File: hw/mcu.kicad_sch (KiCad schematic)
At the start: 2 parts, among them U1 ISP2454-LP-JT

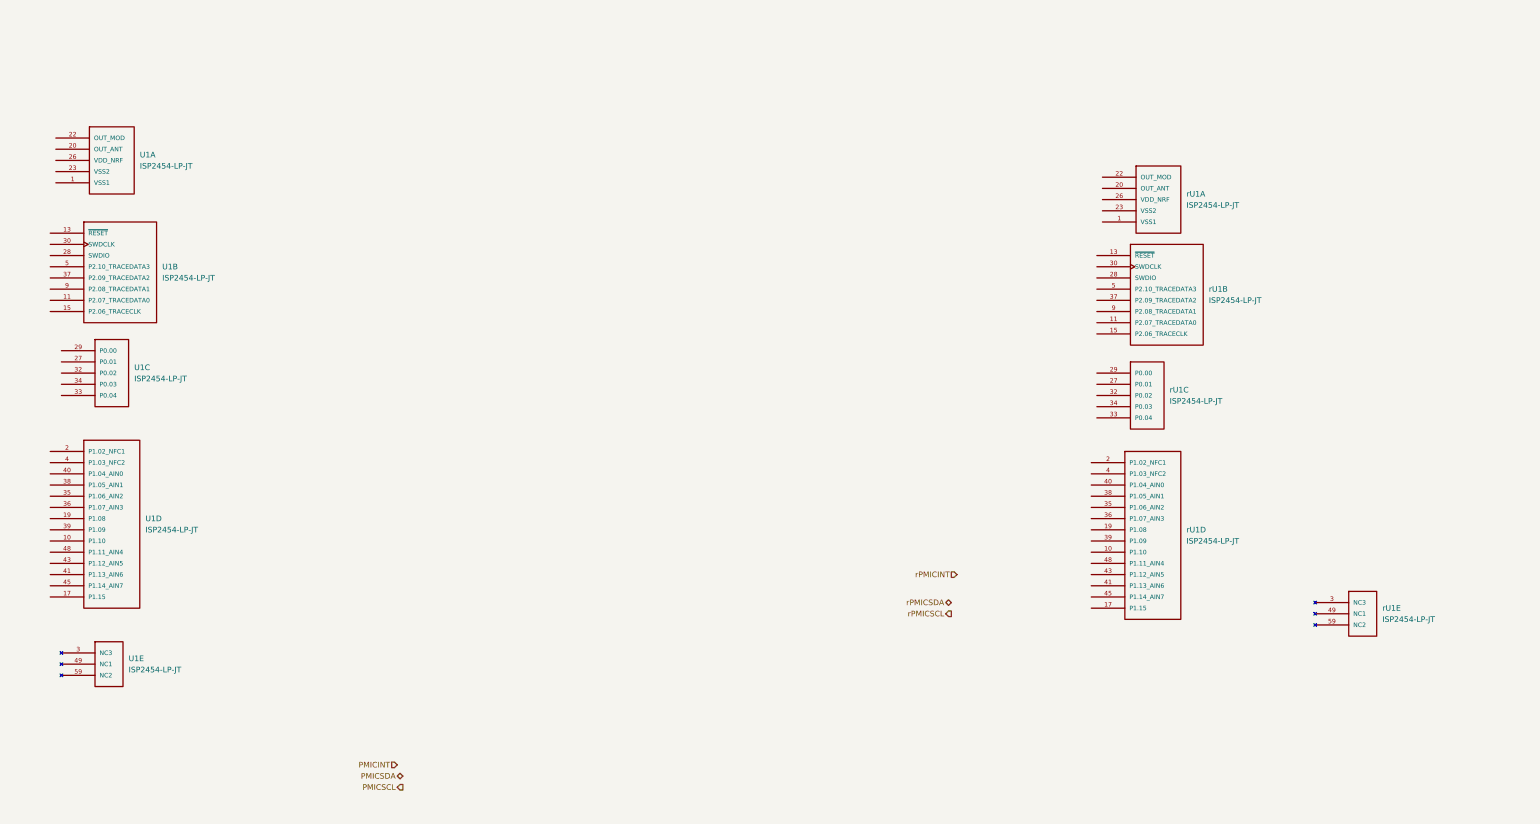
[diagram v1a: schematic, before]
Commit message: Hook up mcu
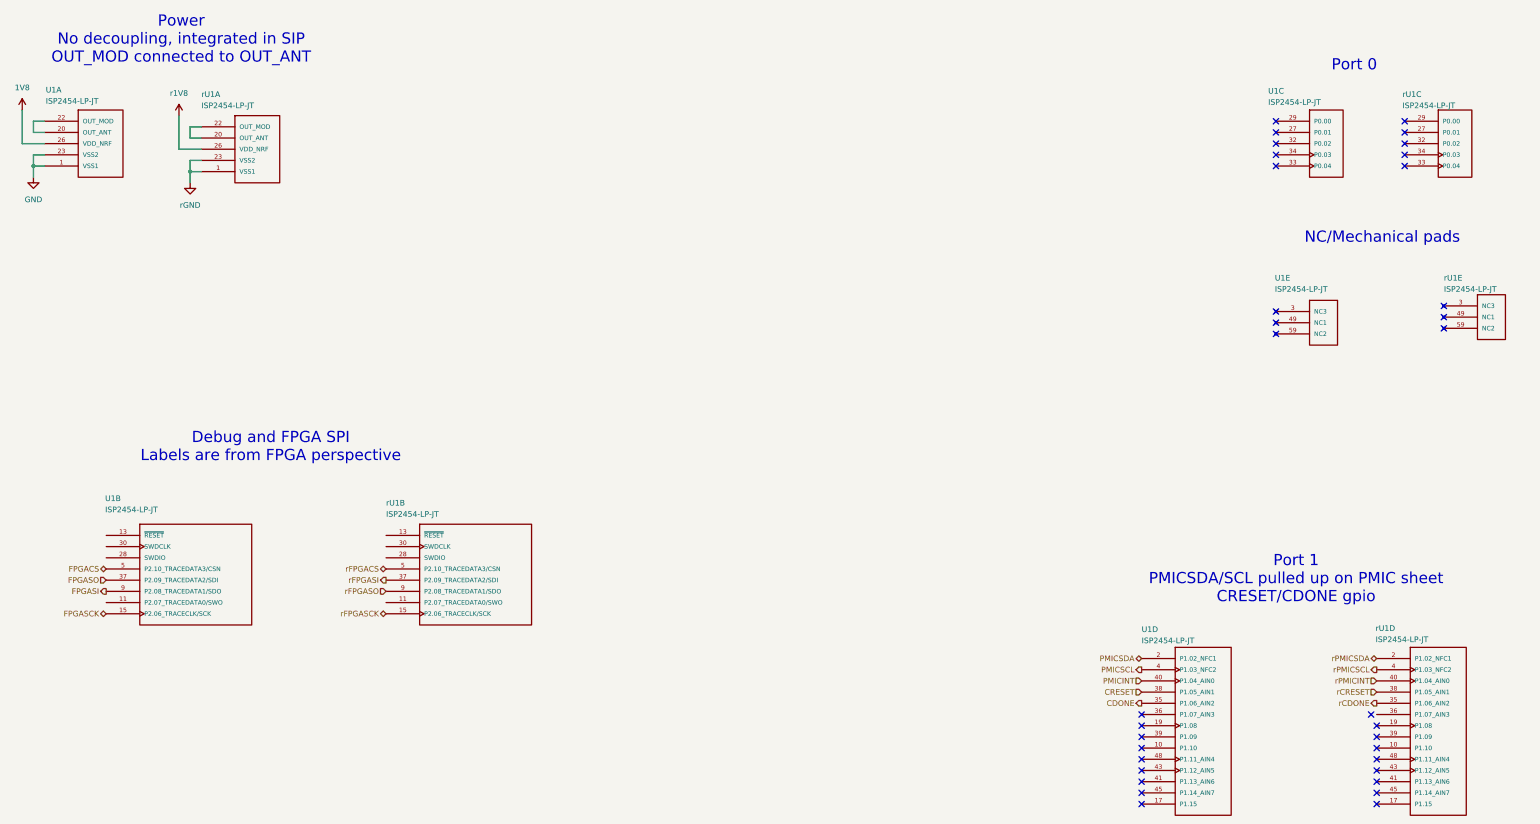
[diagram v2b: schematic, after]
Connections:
- net VSS2 is gone; now on net GND: U1.23 (VSS2), U1.24 (VSS2), U1.25 (VSS2), U1.31 (VSS2), rU1.23 (VSS2), rU1.24 (VSS2), rU1.25 (VSS2), rU1.31 (VSS2)
- net PMICINT: now also U1.40 (P1.04_AIN0)
- net PMICSCL: now also U1.4 (P1.03_NFC2)
- net PMICSDA: now also U1.2 (P1.02_NFC1)
- net rPMICINT: now also rU1.40 (P1.04_AIN0)
- net rPMICSCL: now also rU1.4 (P1.03_NFC2)
- net rPMICSDA: now also rU1.2 (P1.02_NFC1)
- net at rU1.20 (OUT_ANT): now also rU1.22 (OUT_MOD)
- net r1V8: now reaches rU1.26 (VDD_NRF)
- net CDONE: now reaches U1.35 (P1.06_AIN2)
- net CRESET: now reaches U1.38 (P1.05_AIN1)
- net rCDONE: now reaches rU1.35 (P1.06_AIN2)
- net rCRESET: now reaches rU1.38 (P1.05_AIN1)
- net FPGASCK: now reaches U1.15 (P2.06_TRACECLK/SCK)
- net FPGASO: now reaches U1.37 (P2.09_TRACEDATA2/SDI)
- net FPGACS: now reaches U1.5 (P2.10_TRACEDATA3/CSN)
- net FPGASI: now reaches U1.9 (P2.08_TRACEDATA1/SDO)
- net rFPGASCK: now reaches rU1.15 (P2.06_TRACECLK/SCK)
- net rFPGASI: now reaches rU1.37 (P2.09_TRACEDATA2/SDI)
- net rFPGACS: now reaches rU1.5 (P2.10_TRACEDATA3/CSN)
- net rFPGASO: now reaches rU1.9 (P2.08_TRACEDATA1/SDO)
- net at U1.20 (OUT_ANT): now also U1.22 (OUT_MOD)
- net 1V8: now reaches U1.26 (VDD_NRF)
- net VSS1 renamed GND
- no-connect marks 0 -> 34
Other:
- note added: "Debug and FPGA SPI Labels are from FPGA perspective"
- note added: "NC/Mechanical pads"
- note added: "Port 0"
- note added: "Port 1 PMICSDA/SCL pulled up on PMIC sheet CRESET/CDONE gpio"
- note added: "Power No decoupling, integrated in SIP OUT_MOD connected to OUT_ANT"
- moved on the sheet: U1A, U1E, rU1A, rU1E

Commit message: Sheet pins
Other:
- note added: "Port 1 PMICSDA/SCL pulled up on PMIC sheet CRESET/CDONE pulled up on FPGA sheet"
- note removed: "Port 1 PMICSDA/SCL pulled up on PMIC sheet CRESET/CDONE gpio"
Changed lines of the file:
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@@
 		)
 	)
-	(text "Port 1\nPMICSDA/SCL pulled up on PMIC sheet\nCRESET/CDONE gpio"
+	(text "Port 1\nPMICSDA/SCL pulled up on PMIC sheet\nCRESET/CDONE pulled up on FPGA sheet"
 		(exclude_from_sim no)
 		(at 333.502 149.606 0)
@@
 	)
 	(hierarchical_label "rCRESET"
+		(shape output)
+		(at 351.79 175.26 180)
+		(effects
+			(font
+				(size 1.27 1.27)
+			)
+			(justify right)
+		)
+	)
+	(hierarchical_label "CRESET"
+		(shape output)
+		(at 298.45 175.26 180)
+		(effects
+			(font
+				(size 1.27 1.27)
+			)
+			(justify right)
+		)
+	)
+	(hierarchical_label "PMICSCL"
+		(shape output)
+		(at 298.45 170.18 180)
+		(effects
+			(font
+				(size 1.27 1.27)
+			)
+			(justify right)
+		)
+	)
+	(hierarchical_label "rFPGASI"
+		(shape output)
+		(at 127 149.86 180)
+		(effects
+			(font
+				(size 1.27 1.27)
+			)
+			(justify right)
+		)
+	)
+	(hierarchical_label "CDONE"
 		(shape input)
-		(at 351.79 175.26 180)
-		(effects
-			(font
-				(size 1.27 1.27)
-			)
-			(justify right)
-		)
-	)
-	(hierarchical_label "CRESET"
-		(shape input)
-		(at 298.45 175.26 180)
-		(effects
-			(font
-				(size 1.27 1.27)
-			)
-			(justify right)
-		)
-	)
-	(hierarchical_label "PMICSCL"
-		(shape output)
-		(at 298.45 170.18 180)
-		(effects
-			(font
-				(size 1.27 1.27)
-			)
-			(justify right)
-		)
-	)
-	(hierarchical_label "rFPGASI"
-		(shape output)
-		(at 127 149.86 180)
-		(effects
-			(font
-				(size 1.27 1.27)
-			)
-			(justify right)
-		)
-	)
-	(hierarchical_label "CDONE"
-		(shape output)
 		(at 298.45 177.8 180)
 		(effects
@@
 	)
 	(hierarchical_label "rCDONE"
-		(shape output)
+		(shape input)
 		(at 351.79 177.8 180)
 		(effects

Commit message: Debug header
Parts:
- added J3, rJ3: TC2050-IDC, Alidade:TAG-CONNECT_TC2050-IDC, symbol Alidade:TC2050-IDC
- added R15, R16, R17, rR15, rR16, rR17: 10k, symbol Alidade:R
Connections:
- net 1V8: now also J3.1 (VREF), R15.1, R16.1
- net GND: now also J3.3 (GND), J3.5 (GND), J3.9 (GND), R17.2, rJ3.3 (GND), rJ3.5 (GND), rJ3.9 (GND), rR17.2
- net r1V8: now also rJ3.1 (VREF), rR15.1, rR16.1
- net SWO: now reaches U1.11 (P2.07_TRACEDATA0/SWO)
- net SWO: now also J3.6 (SWO)
- net NRST: now reaches U1.13 (~{RESET})
- net NRST: now also J3.10 (nRST), R16.2
- net SWDIO: now reaches U1.28 (SWDIO)
- net SWDIO: now also J3.2 (SWDIO), R15.2
- net SWCLK: now reaches U1.30 (SWDCLK)
- net SWCLK: now also J3.4 (SWDCLK), R17.1
- net rSWO: now reaches rU1.11 (P2.07_TRACEDATA0/SWO)
- net rSWO: now also rJ3.6 (SWO)
- net rNRST: now reaches rU1.13 (~{RESET})
- net rNRST: now also rJ3.10 (nRST), rR16.2
- net rSWDIO: now reaches rU1.28 (SWDIO)
- net rSWDIO: now also rJ3.2 (SWDIO), rR15.2
- net rSWCLK: now reaches rU1.30 (SWDCLK)
- net rSWCLK: now also rJ3.4 (SWDCLK), rR17.1
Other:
- note added: "Debug Header Pull up SWDIO, NRST Pull down SWCLK"
- title: (none) -> Alidade
- moved on the sheet: U1B, rU1B

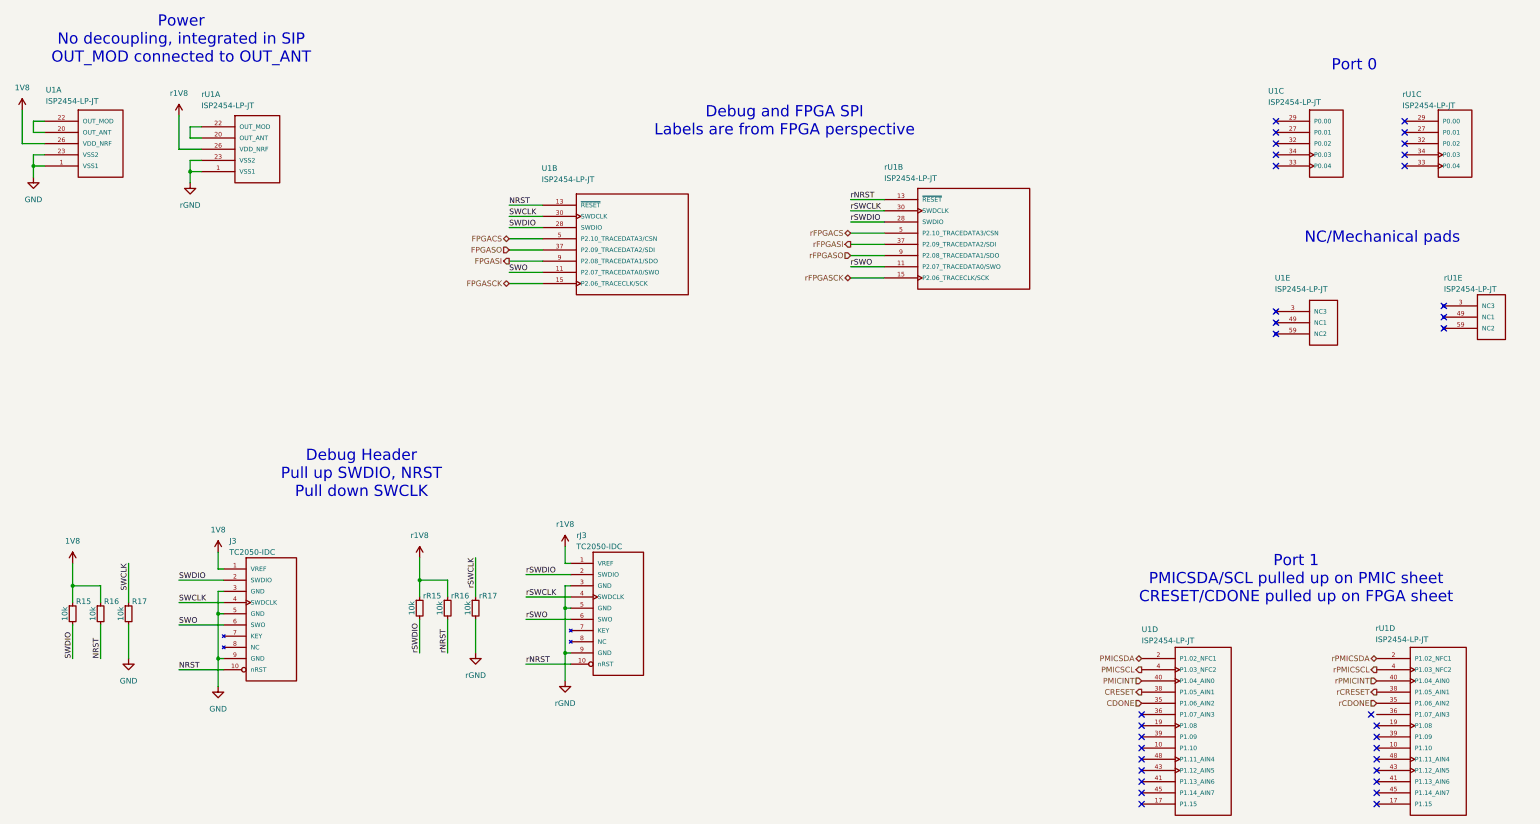
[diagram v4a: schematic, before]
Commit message: mcu page erc
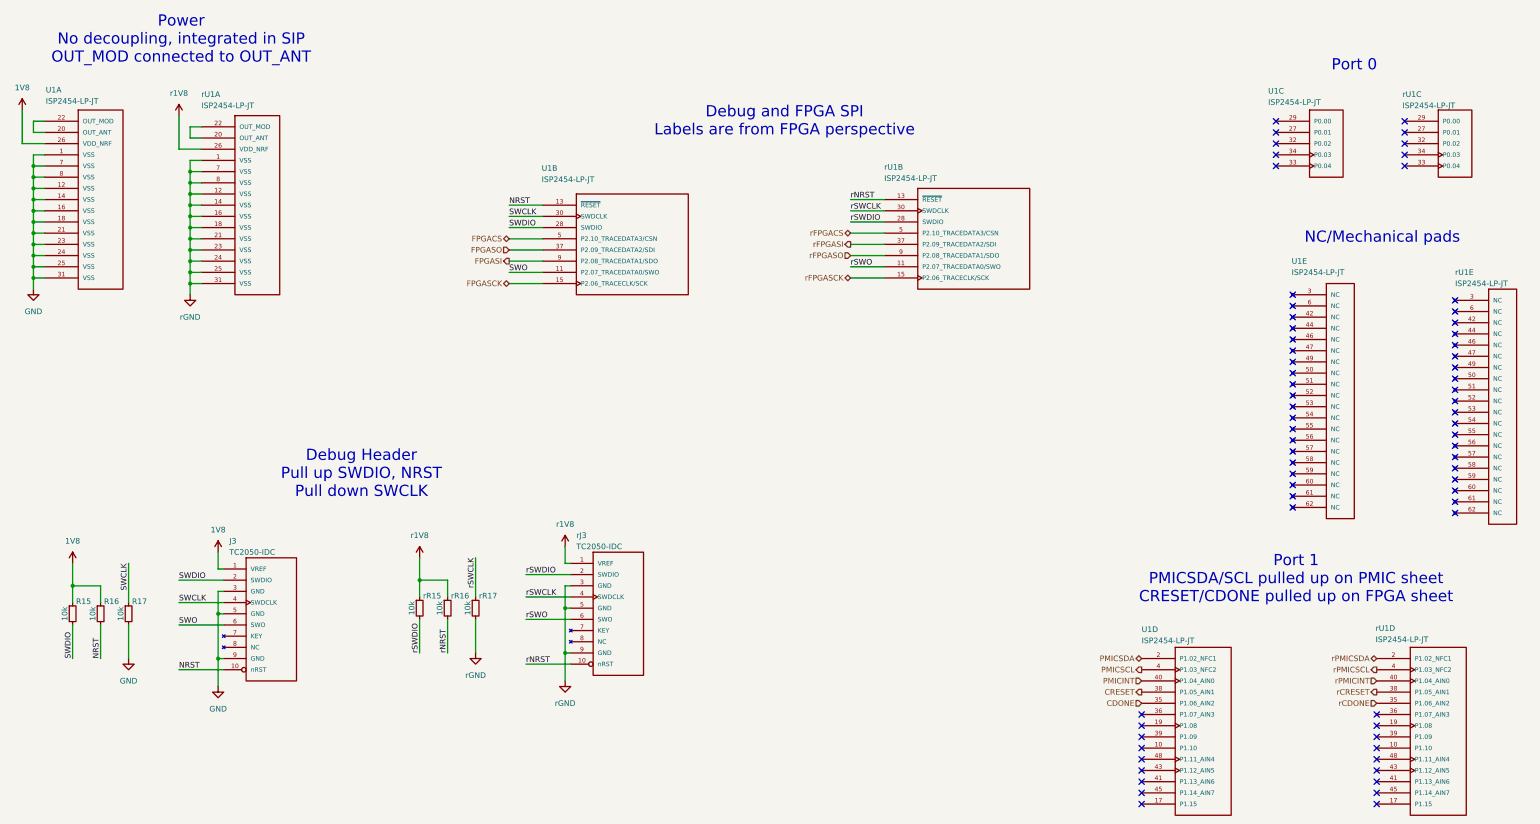
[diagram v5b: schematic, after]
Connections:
- net GND: no longer rJ3.3 (GND), rJ3.5 (GND), rJ3.9 (GND), rR17.2, rU1.1 (VSS1), rU1.12 (VSS1), rU1.14 (VSS1), rU1.16 (VSS1), rU1.18 (VSS1), rU1.21 (VSS1), rU1.23 (VSS2), rU1.24 (VSS2), rU1.25 (VSS2), rU1.31 (VSS2), rU1.7 (VSS1), rU1.8 (VSS1)
- new net rGND: rJ3.3 (GND), rJ3.5 (GND), rJ3.9 (GND), rR17.2, rU1.1 (VSS), rU1.12 (VSS), rU1.14 (VSS), rU1.16 (VSS), rU1.18 (VSS), rU1.21 (VSS), rU1.23 (VSS), rU1.24 (VSS), rU1.25 (VSS), rU1.31 (VSS), rU1.7 (VSS), rU1.8 (VSS)
- now unconnected: U1.3 (NC3), U1.42 (NC3), U1.44 (NC3), U1.46 (NC3), U1.47 (NC3), U1.49 (NC1), U1.50 (NC1), U1.51 (NC1), U1.52 (NC1), U1.53 (NC1), U1.54 (NC1), U1.55 (NC1), U1.56 (NC1), U1.57 (NC1), U1.58 (NC1), U1.59 (NC2), U1.6 (NC3), U1.60 (NC2), U1.61 (NC2), U1.62 (NC2), rU1.3 (NC3), rU1.42 (NC3), rU1.44 (NC3), rU1.46 (NC3), rU1.47 (NC3), rU1.49 (NC1), rU1.50 (NC1), rU1.51 (NC1), rU1.52 (NC1), rU1.53 (NC1), rU1.54 (NC1), rU1.55 (NC1), rU1.56 (NC1), rU1.57 (NC1), rU1.58 (NC1), rU1.59 (NC2), rU1.6 (NC3), rU1.60 (NC2), rU1.61 (NC2), rU1.62 (NC2)
- no-connect marks 34 -> 68
